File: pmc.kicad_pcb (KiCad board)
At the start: 6 copper layers, 47 x 45.1 mm, 143 parts, among them M1 LM46001, M2 TPS61040, M3 STM32F405RG, M4 REF3033, M5 TPS73633, M6 SN65HVD233, M7 UCC27211A, M8 UCC27211A, M9 UCC27211A, P1 BOOT, P10 CONN4, P11 DEBUG, P2 PWM, P3 HALL, P4 SPI, P5 CAN, P6 CONN4, P7 CONN4, P8 CONN4, P9 CONN4, Q1 BC857C, Q2 IPT007N06N, Q3 IPT007N06N, Q4 IPT007N06N, Q5 IPT007N06N, Q6 IPT007N06N, Q7 IPT007N06N, U1 AD8539, U2 AD8539, U3 AD8417, U4 AD8417

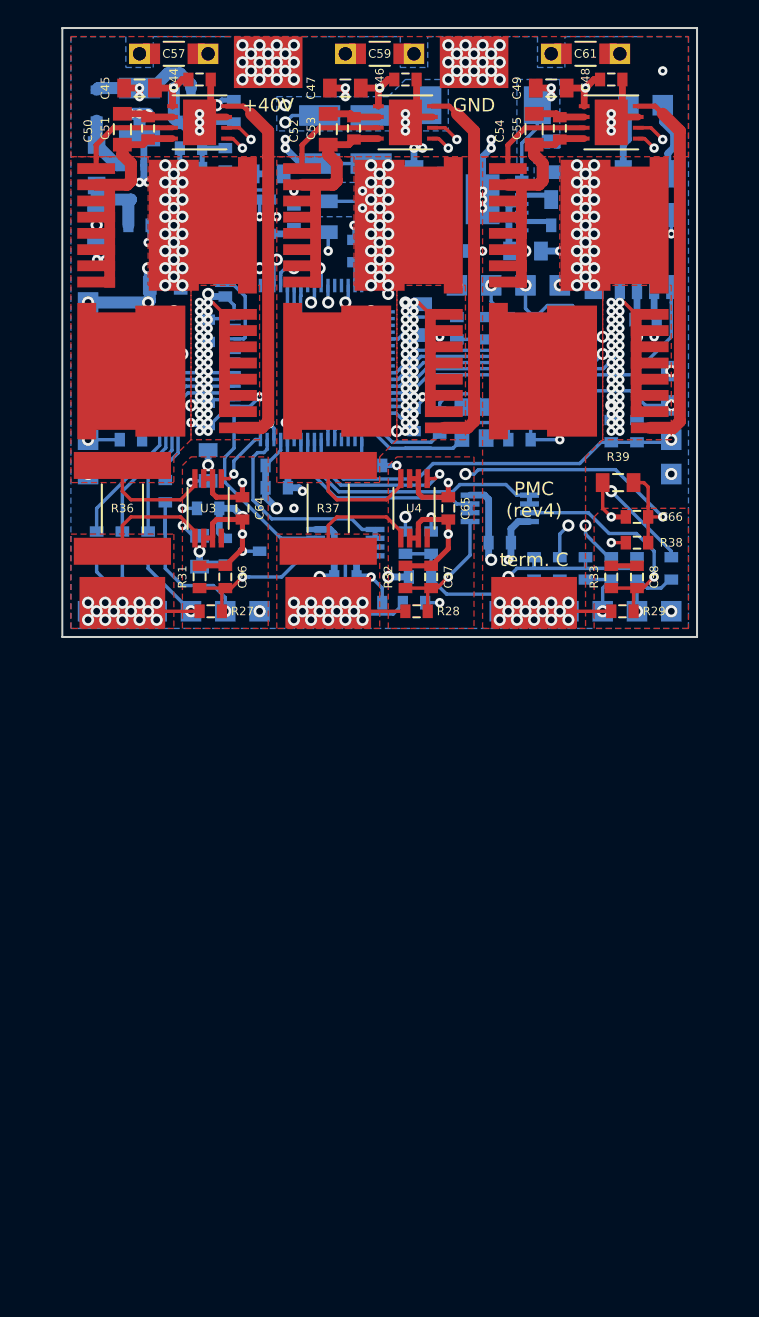
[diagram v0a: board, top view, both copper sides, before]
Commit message: A new design with two 6-layer pcbs.
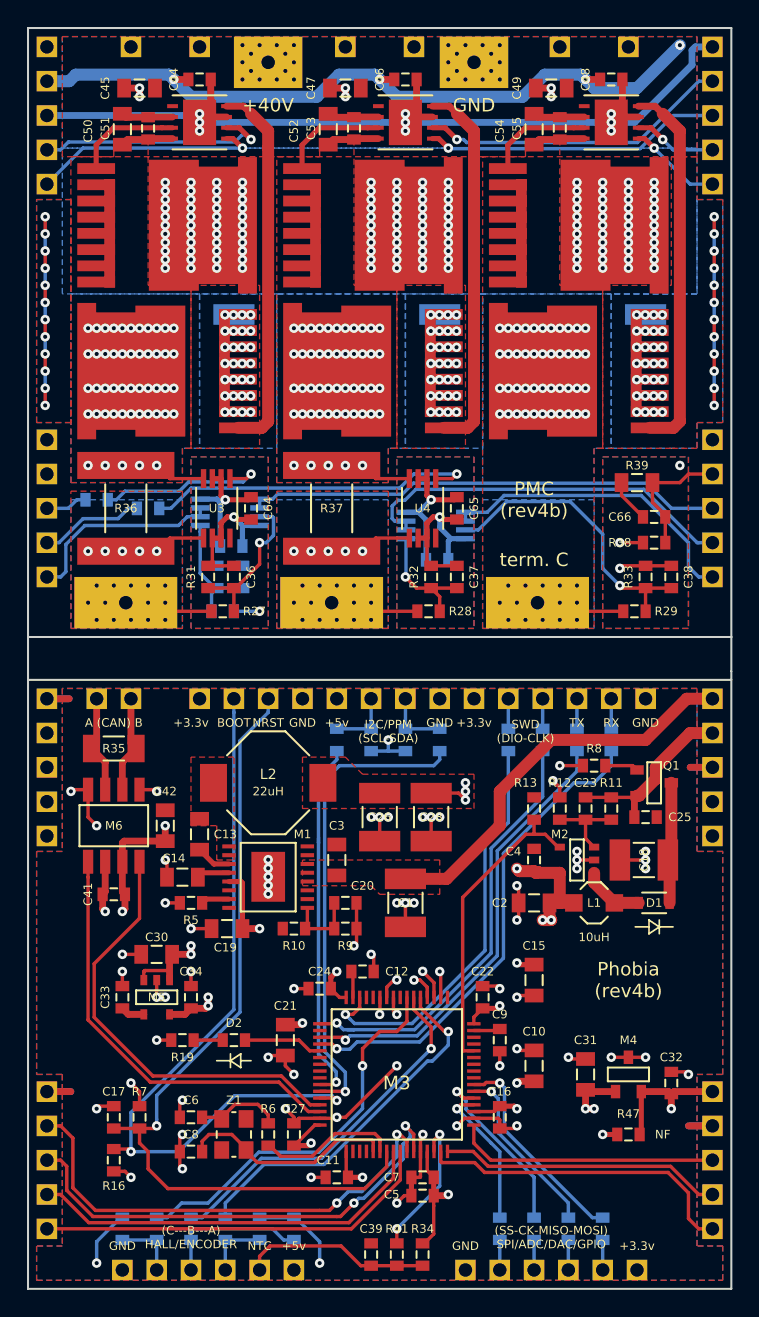
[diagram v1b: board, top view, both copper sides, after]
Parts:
- added P12: F1, foot:PLS-5, F.Cu at (111.0, 122.0)
- added P13: F2, foot:PLS-5, F.Cu at (61.7, 122.0)
- added P14: A1, foot:PLS-5, F.Cu at (111.0, 151.1)
- added P15: A2, foot:PLS-5, F.Cu at (61.7, 151.1)
- added P16: F1, foot:PLS-5, F.Cu at (61.7, 73.8)
- added P17: F2, foot:PLS-5, F.Cu at (111.0, 73.8)
- added P18: A1, foot:PLS-5, F.Cu at (61.7, 102.9)
- added P19: A2, foot:PLS-5, F.Cu at (111.0, 102.9)
- added R45: 1K 1%, foot:SM-0603, B.Cu at (69.2, 102.9)
- added R46: 1K 1%, foot:SM-0603, B.Cu at (65.4, 102.2)
- added R47: NF, foot:SM-0603, F.Cu at (104.8, 149.2)
- C1: value 100nF 100v -> 2.2uF 100v; footprint foot:SM-0805 -> foot:SM-1210; moved to F.Cu
- C10, C11, C12, C13, C14, C15, C16, C17, C18, C19, C2, C20, C21, C22, C23, C24, C25, C26, C27, C28, C3, C30, C31, C32, C33, C34, C39, C4, C41, C42, C5, C56, C6, C60, C7, C8, C9, D1, D2, L1, L2, M1, M2, M3, M4, M5, M6, Q1, R10, R11, R12, R13, R16, R19, R34, R35, R41, R5, R6, R7, R8, R9, Z1: moved to F.Cu
- C57, C59, C61: footprint foot:SM-1206 -> foot:SM-1210; moved to B.Cu
- P1, P2: footprint foot:PAD-4 -> foot:PLS-4; moved to F.Cu
- P11, P3, P4: footprint foot:PAD-6 -> foot:PLS-6; moved to F.Cu
- P5: footprint foot:PAD-2 -> foot:PLS-2; moved to F.Cu
- moved D1 72.0 mm to (106.7, 132.1), turned to 180 degrees
- moved C18 66.8 mm to (105.9, 128.9), turned to 180 degrees
- moved L1 65.9 mm to (102.2, 132.1), turned to 0 degrees
- moved R16 65.4 mm to (66.7, 151.1)
- moved C17 63.9 mm to (66.7, 148.0)
- moved R4 63.1 mm to (102.9, 156.2)
- moved R22 62.0 mm to (69.8, 156.2)
- moved R25 62.0 mm to (67.3, 156.2)
- moved R7 61.6 mm to (68.6, 148.0)
- moved Q1 60.8 mm to (106.7, 123.2), turned to 270 degrees
- moved R3 60.6 mm to (100.3, 156.2)
- moved R1 60.0 mm to (95.2, 156.2)
- moved C2 59.7 mm to (97.8, 132.1), turned to 180 degrees
- moved M2 59.5 mm to (101.0, 128.9), turned to 90 degrees
- moved C33 59.2 mm to (67.3, 139.1)
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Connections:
- C39 pad 2: Net-(C39-Pad2) -> EXT_NTC
- D2 pad 1: GND -> Net-(D2-Pad1)
- D2 pad 2: Net-(D2-Pad2) -> LED
- M3 pad 10: VOLTAGE_B -> ADC_IN12
- M3 pad 11: PCB_NTC -> ADC_IN13
- M3 pad 14: EXT_NTC -> Net-(M3-Pad14)
- M3 pad 15: VOLTAGE_U -> ADC_IN1
- M3 pad 16: CURRENT_A -> ADC_IN2
- M3 pad 17: VOLTAGE_A -> ADC_IN3
- M3 pad 34: FET_AL -> TIM1_CH1N
- M3 pad 35: FET_BL -> TIM1_CH2N
- M3 pad 36: FET_CL -> TIM1_CH3N
- M3 pad 41: FET_AH -> TIM1_CH1
- M3 pad 42: FET_BH -> TIM1_CH2
- M3 pad 43: FET_CH -> TIM1_CH3
- M3 pad 8: CURRENT_B -> ADC_IN10
- M3 pad 9: VOLTAGE_C -> ADC_IN11
- P3 pad 2: Net-(C39-Pad2) -> EXT_NTC
- R19 pad 1: LED -> Net-(D2-Pad1)
- R19 pad 2: Net-(D2-Pad2) -> GND
- R34 pad 1: Net-(C39-Pad2) -> EXT_NTC
- R41 pad 1: Net-(C39-Pad2) -> Net-(M3-Pad14)
- U1 pad 1: VOLTAGE_U -> VOLTAGE_A
- U1 pad 2: VOLTAGE_U -> VOLTAGE_A
- U1 pad 3: Net-(C35-Pad1) -> Net-(C36-Pad1)
- U1 pad 5: Net-(C36-Pad1) -> Net-(C35-Pad1)
- U1 pad 6: VOLTAGE_A -> VOLTAGE_U
- U1 pad 7: VOLTAGE_A -> VOLTAGE_U
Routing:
- net GND: track 258.4 -> 348.4 mm
- net +3.3VREF: track 35.0 -> 105.7 mm, vias 8 -> 5
- net +36V: track 131.4 -> 192.0 mm, vias 91 -> 147
- net TIM1_CH2N: track 0.00 -> 37.4 mm, vias 0 -> 1
- net TIM1_CH3N: track 0.00 -> 36.5 mm, vias 0 -> 1
- net ADC_IN13: track 0.00 -> 35.9 mm, vias 0 -> 2
- net TIM1_CH3: track 0.00 -> 35.7 mm, vias 0 -> 1
- net ADC_IN12: track 0.00 -> 35.7 mm, vias 0 -> 2
- net TIM1_CH2: track 0.00 -> 35.3 mm, vias 0 -> 1
- net TIM1_CH1: track 0.00 -> 34.7 mm, vias 0 -> 1
- net NRST: track 29.1 -> 61.6 mm
- net FET_CL: track 36.3 -> 6.17 mm, vias 2 -> 1
- net TIM1_CH1N: track 0.00 -> 30.0 mm, vias 0 -> 1
- net ADC_IN10: track 0.00 -> 29.9 mm
- net ADC_IN11: track 0.00 -> 29.8 mm
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- added copper zone on In2.Cu, net +3.3V
- added copper zone on In4.Cu, net +3.3VREF
- added copper zone on F.Cu, net +36V
- added copper zone on In4.Cu, net +36V
- added copper zone on F.Cu, net +5V
- added copper zone on In4.Cu, net +5V
- added copper zone on In3.Cu, net GND
- added copper zone on F.Cu, net Net-(C13-Pad1)
- added copper zone on B.Cu, net Net-(C50-Pad1)
- added copper zone on In2.Cu, net Net-(C50-Pad1)
- added copper zone on In4.Cu, net Net-(C50-Pad1)
- added copper zone on B.Cu, net Net-(C52-Pad1)
- added copper zone on In2.Cu, net Net-(C52-Pad1)
- added copper zone on In4.Cu, net Net-(C52-Pad1)
- added copper zone on B.Cu, net TERMINAL_A
- added copper zone on In4.Cu, net TERMINAL_A
- added copper zone on B.Cu, net TERMINAL_B
- added copper zone on In4.Cu, net TERMINAL_B
- added copper zone on B.Cu, net TERMINAL_C
- added copper zone on In4.Cu, net TERMINAL_C
- removed copper zone on In3.Cu, net +3.3V
- removed copper zone on In2.Cu, net +3.3VREF
- removed copper zone on In3.Cu, net +3.3VREF
- removed copper zone on B.Cu, net +5V
- removed copper zone on In3.Cu, net +5V
- removed copper zone on B.Cu, net Net-(C13-Pad1)
- removed copper zone on In1.Cu, net TERMINAL_A
- removed copper zone on In1.Cu, net TERMINAL_B
- removed copper zone on In1.Cu, net TERMINAL_C
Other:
- board size 47 x 45.1 mm -> 52.1 x 93.3 mm
- board text added: "(C---B---A) HALL/ENCODER"
- board text added: "(SS-CK-MISO-MOSI) SPI/ADC/DAC/GPIO"
- board text added: "+3.3v"
- board text added: "+5v"
- board text added: "10uH"
- board text added: "22uH"
- board text added: "A (CAN) B"
- board text added: "I2C/PPM (SCL-SDA)"
- board text added: "NRST"
- board text added: "PMC (rev4b)"
- board text added: "Phobia (rev4b)"
- board text added: "SWD (DIO-CLK)"
- board text removed: "+3.3V"
- board text removed: "+5V"
- board text removed: "A"
- board text removed: "B"
- board text removed: "C"
- board text removed: "H"
- board text removed: "L"
- board text removed: "MISO"
- board text removed: "MOSI"
- board text removed: "NSS"
- board text removed: "PMC (rev4)"
- board text removed: "R4"
- board text removed: "SCK"
- board text removed: "SCL"
- board text removed: "SDA"
- board text removed: "SWCLK"
- board text removed: "SWDIO"

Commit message: Fixed routing of control pcb.
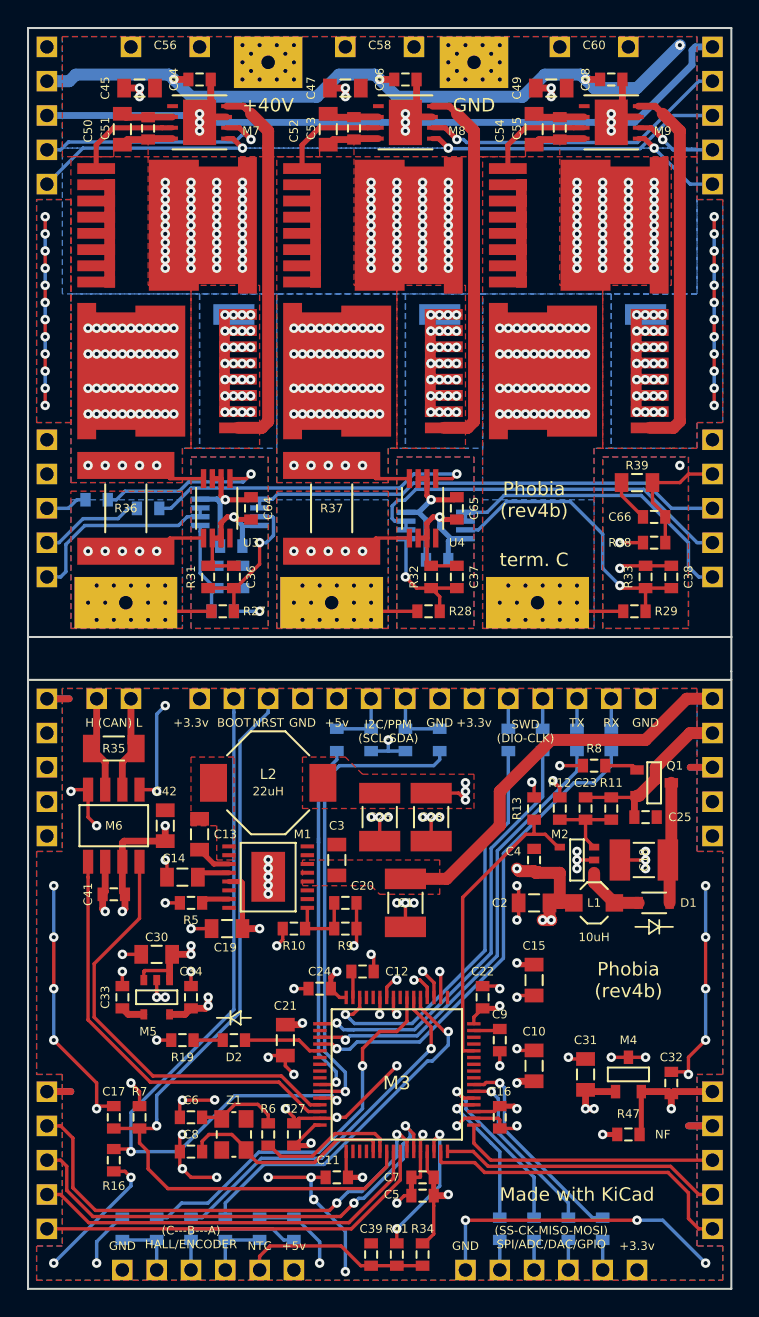
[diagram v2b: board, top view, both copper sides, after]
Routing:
- net GND: track 348.4 -> 437.9 mm, vias 202 -> 222
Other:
- board text added: "H (CAN) L"
- board text added: "Made with KiCad"
- board text removed: "A (CAN) B"
- board text removed: "PMC (rev4b)"

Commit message: Added analog input and FAN output.
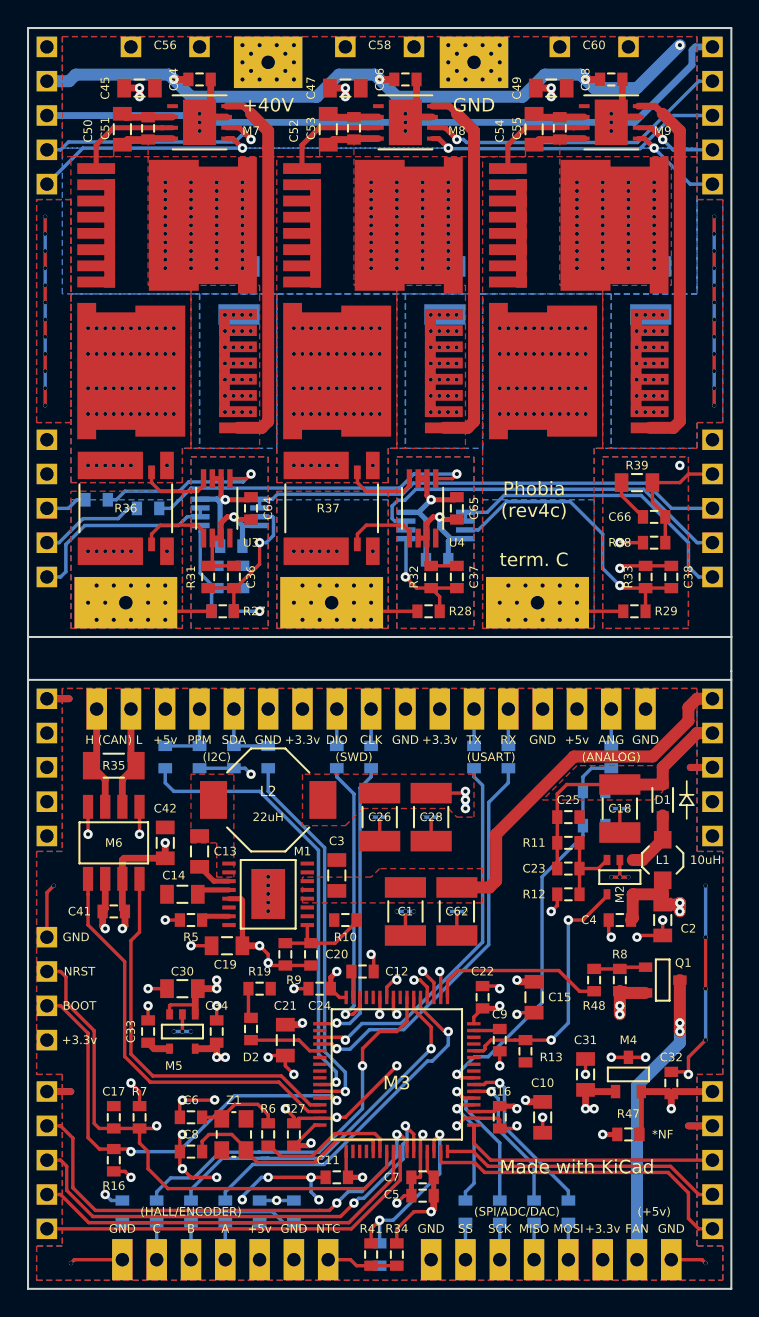
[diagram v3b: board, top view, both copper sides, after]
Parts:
- added C29: 10nF 25v, foot:SM-0603, B.Cu at (102.2, 126.4)
- added C62: 2.2uF 100v, foot:SM-1210, F.Cu at (92.1, 132.7)
- added P20: ANALOG, foot:PLS-3, F.Cu at (103.5, 117.7)
- added P21: SWD, foot:PLS-4, F.Cu at (84.5, 117.7)
- added P22: USART, foot:PLS-4, F.Cu at (94.6, 117.7)
- added P23: HALL, foot:PLS-5, F.Cu at (72.4, 158.5)
- added R48: 1K, foot:SM-0603, F.Cu at (102.2, 137.8)
- added R49: 10K 1%, foot:SM-0603, B.Cu at (102.2, 123.8)
- added R50: 10K 1%, foot:SM-0603, B.Cu at (103.5, 121.3)
- C39: moved to B.Cu
- P11: value DEBUG -> FAN; footprint foot:PLS-6 -> foot:PLS-2
- P2: value PWM -> PPM
- P3: value HALL -> NTC; footprint foot:PLS-6 -> foot:PLS-2
- Q1: value BC857C -> IRLML6401
- R10: value 27K 1% -> 25.5K 1%
- R12: value 11K 1% -> 11.3K 1%
- R36, R37: value 0.0005 1% -> 0.0003 1%; footprint foot:LR2512-D -> foot:LR2512-4
- R41: value 1K -> 10K
- R47: value NF -> *NF
- moved P11 42.1 mm to (106.7, 158.5)
- moved P1 26.3 mm to (61.7, 138.4), turned to 90 degrees
- moved R13 18.0 mm to (97.2, 143.1), turned to 90 degrees
- moved R8 16.0 mm to (104.1, 137.8), turned to 90 degrees
- moved Q1 14.6 mm to (107.3, 137.8)
- moved R14 12.8 mm to (83.2, 121.3)
- moved R17 12.8 mm to (85.7, 121.3)
- moved R40 12.8 mm to (70.5, 121.3)
- moved R42 12.8 mm to (78.1, 121.3)
- moved R44 12.8 mm to (75.6, 121.3)
- moved R43 12.8 mm to (73.0, 121.3)
- moved P2 12.7 mm to (74.3, 117.7)
- moved C2 9.61 mm to (107.3, 133.3), turned to 270 degrees
- moved C4 7.75 mm to (104.1, 133.3), turned to 180 degrees
- moved R15 7.73 mm to (93.3, 121.3)
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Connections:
- C18 pad 1: Net-(C18-Pad1) -> +12V
- C39 pad 2: EXT_NTC -> Net-(C39-Pad2)
- D1 pad 1: Net-(C18-Pad1) -> +12V
- M3 pad 14: Net-(M3-Pad14) -> Net-(C39-Pad2)
- M3 pad 24: (no net) -> ADC_IN14
- M3 pad 33: (no net) -> FAN
- P11 pad 1: +3.3V -> Net-(P11-Pad1)
- P11 pad 2: SWDIO -> GND
- P3 pad 1: +5V -> EXT_NTC
- P3 pad 2: EXT_NTC -> GND
- Q1 pad 2: +12V -> +5V
- Q1 pad 3: Net-(C18-Pad1) -> Net-(P11-Pad1)
- R36 pad 1: TERMINAL_A -> Net-(C50-Pad1)
- R36 pad 2: Net-(C50-Pad1) -> TERMINAL_A
- R37 pad 1: TERMINAL_B -> Net-(C52-Pad1)
- R37 pad 2: Net-(C52-Pad1) -> TERMINAL_B
- R41 pad 1: Net-(M3-Pad14) -> Net-(C39-Pad2)
- U3 pad 1: TERMINAL_A -> Net-(R36-Pad4)
- U3 pad 8: Net-(C50-Pad1) -> Net-(R36-Pad3)
- U4 pad 1: TERMINAL_B -> Net-(R37-Pad4)
- U4 pad 8: Net-(C52-Pad1) -> Net-(R37-Pad3)
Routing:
- net GND: track 437.9 -> 386.2 mm, vias 222 -> 215
- net ADC_IN14: track 0.00 -> 30.2 mm, vias 0 -> 1
- net BOOT: track 56.5 -> 33.6 mm
- net Net-(P11-Pad1): track 0.00 -> 22.7 mm, vias 0 -> 2
- net NRST: track 61.6 -> 41.5 mm
- net Net-(C39-Pad2): track 0.00 -> 13.9 mm, vias 0 -> 2
- net FAN: track 0.00 -> 13.0 mm
- net Net-(M3-Pad14): track 10.8 -> 0.00 mm, vias 2 -> 0
- net Net-(M3-Pad49): track 32.3 -> 21.8 mm
- net Net-(M3-Pad46): track 30.4 -> 21.0 mm
- net Net-(C18-Pad1): track 9.05 -> 0.00 mm
- net EXT_NTC: track 14.0 -> 5.26 mm
- net Net-(M3-Pad59): track 35.4 -> 28.2 mm
- net Net-(M3-Pad52): track 36.1 -> 29.5 mm
- net Net-(M3-Pad58): track 27.3 -> 33.5 mm
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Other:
- rule via_min_size: 0.7 -> 0.3
- board text added: "(+5v)"
- board text added: "(ANALOG)"
- board text added: "(HALL/ENCODER)"
- board text added: "(I2C)"
- board text added: "(SPI/ADC/DAC)"
- board text added: "(SWD)"
- board text added: "(USART)"
- board text added: "A"
- board text added: "ANG"
- board text added: "B"
- board text added: "C"
- board text added: "CLK"
- board text added: "DIO"
- board text added: "FAN"
- board text added: "MISO"
- board text added: "MOSI"
- board text added: "PPM"
- board text added: "Phobia (rev4c)"
- board text added: "SCK"
- board text added: "SDA"
- board text added: "SS"
- board text removed: "(C---B---A) HALL/ENCODER"
- board text removed: "(SS-CK-MISO-MOSI) SPI/ADC/DAC/GPIO"
- board text removed: "I2C/PPM (SCL-SDA)"
- board text removed: "Phobia (rev4b)"
- board text removed: "SWD (DIO-CLK)"

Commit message: Improved step-up layout.
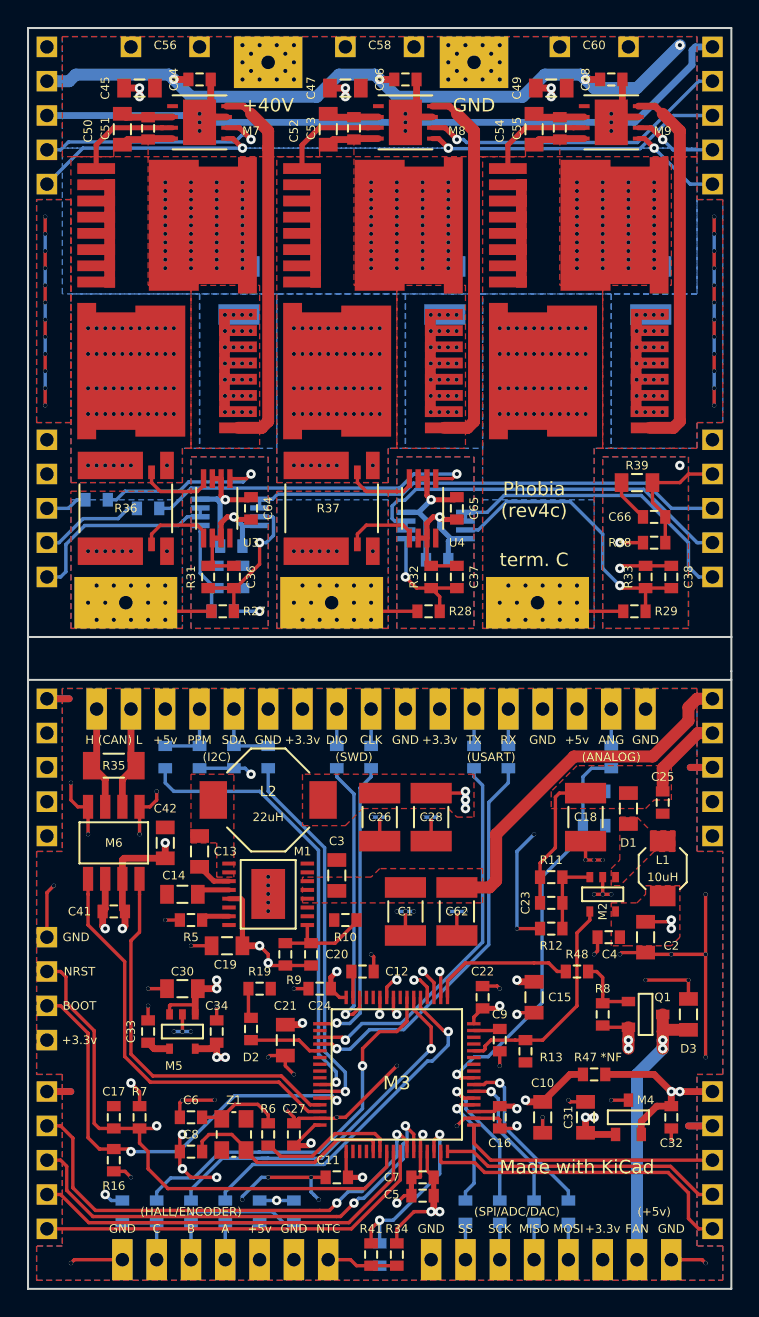
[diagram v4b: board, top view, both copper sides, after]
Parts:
- added D3: NSR0320, foot:SM-0805, F.Cu at (109.2, 140.3)
- C35, C36, C37, C38: value 120pF -> 47pF C0G
- D1: footprint foot:SOD-232 -> foot:SM-0805
- moved C25 7.07 mm to (107.3, 124.7), turned to 270 degrees
- moved R47 5.12 mm to (102.2, 144.8)
- moved C31 3.18 mm to (101.6, 148.0)
- moved M4 3.18 mm to (104.8, 148.0)
- moved C23 2.84 mm to (99.1, 132.1)
- moved Q1 2.84 mm to (106.0, 140.3)
- moved R12 2.84 mm to (99.1, 134.0)
- moved R8 2.84 mm to (102.9, 140.3)
- moved R11 2.84 mm to (99.1, 130.2)
- moved C18 2.62 mm to (101.6, 125.7)
- moved D1 2.62 mm to (104.8, 125.1)
- moved C32 2.54 mm to (108.0, 148.0), turned to 270 degrees
- moved C2 1.80 mm to (106.0, 134.6)
- moved M2 1.80 mm to (102.9, 131.4)
- moved C4 1.51 mm to (103.3, 134.6)
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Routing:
- net GND: track 386.2 -> 402.6 mm, vias 215 -> 218
- net +3.3VREF: track 107.8 -> 113.7 mm, vias 5 -> 7
- net +5V: track 41.5 -> 35.8 mm
- net Net-(D1-Pad2): track 4.65 -> 0.00 mm
- net +12V: track 74.7 -> 71.7 mm
- net 12V_EN: track 19.3 -> 16.5 mm, vias 2 -> 0
- net +3.3V: track 40.1 -> 42.9 mm, vias 15 -> 14
- net FAN: track 13.0 -> 10.8 mm
- net Net-(Q1-Pad1): track 3.86 -> 5.13 mm
- net Net-(D3-Pad1): track 22.7 -> 21.5 mm
- added copper zone on F.Cu, net Net-(D1-Pad2)
